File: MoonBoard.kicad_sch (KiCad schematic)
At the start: 26 parts, among them SW1 SW_SPST, U1 AMS1117-3.3, U2 STM32F446RETx, U9 SN74LV1T34DBV, Y1 25MHz

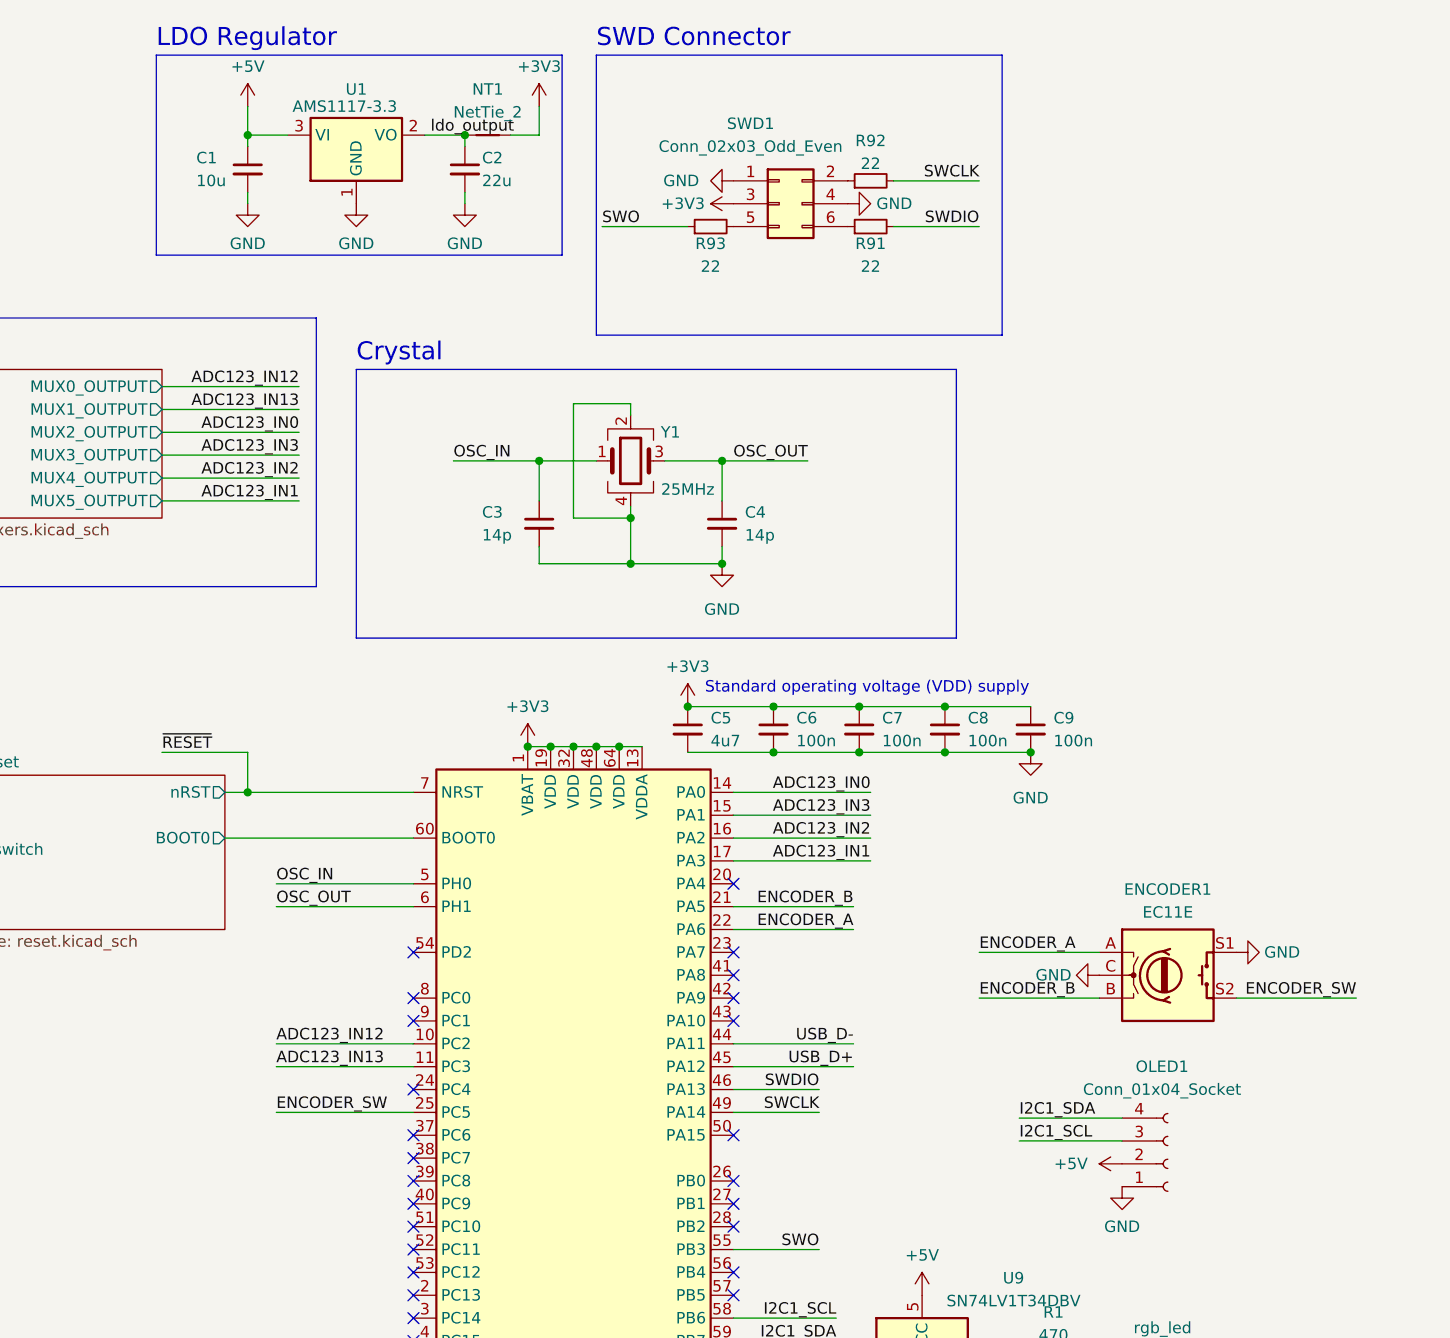
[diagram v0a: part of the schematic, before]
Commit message: fix LED footprint, add boot/reset jumpers
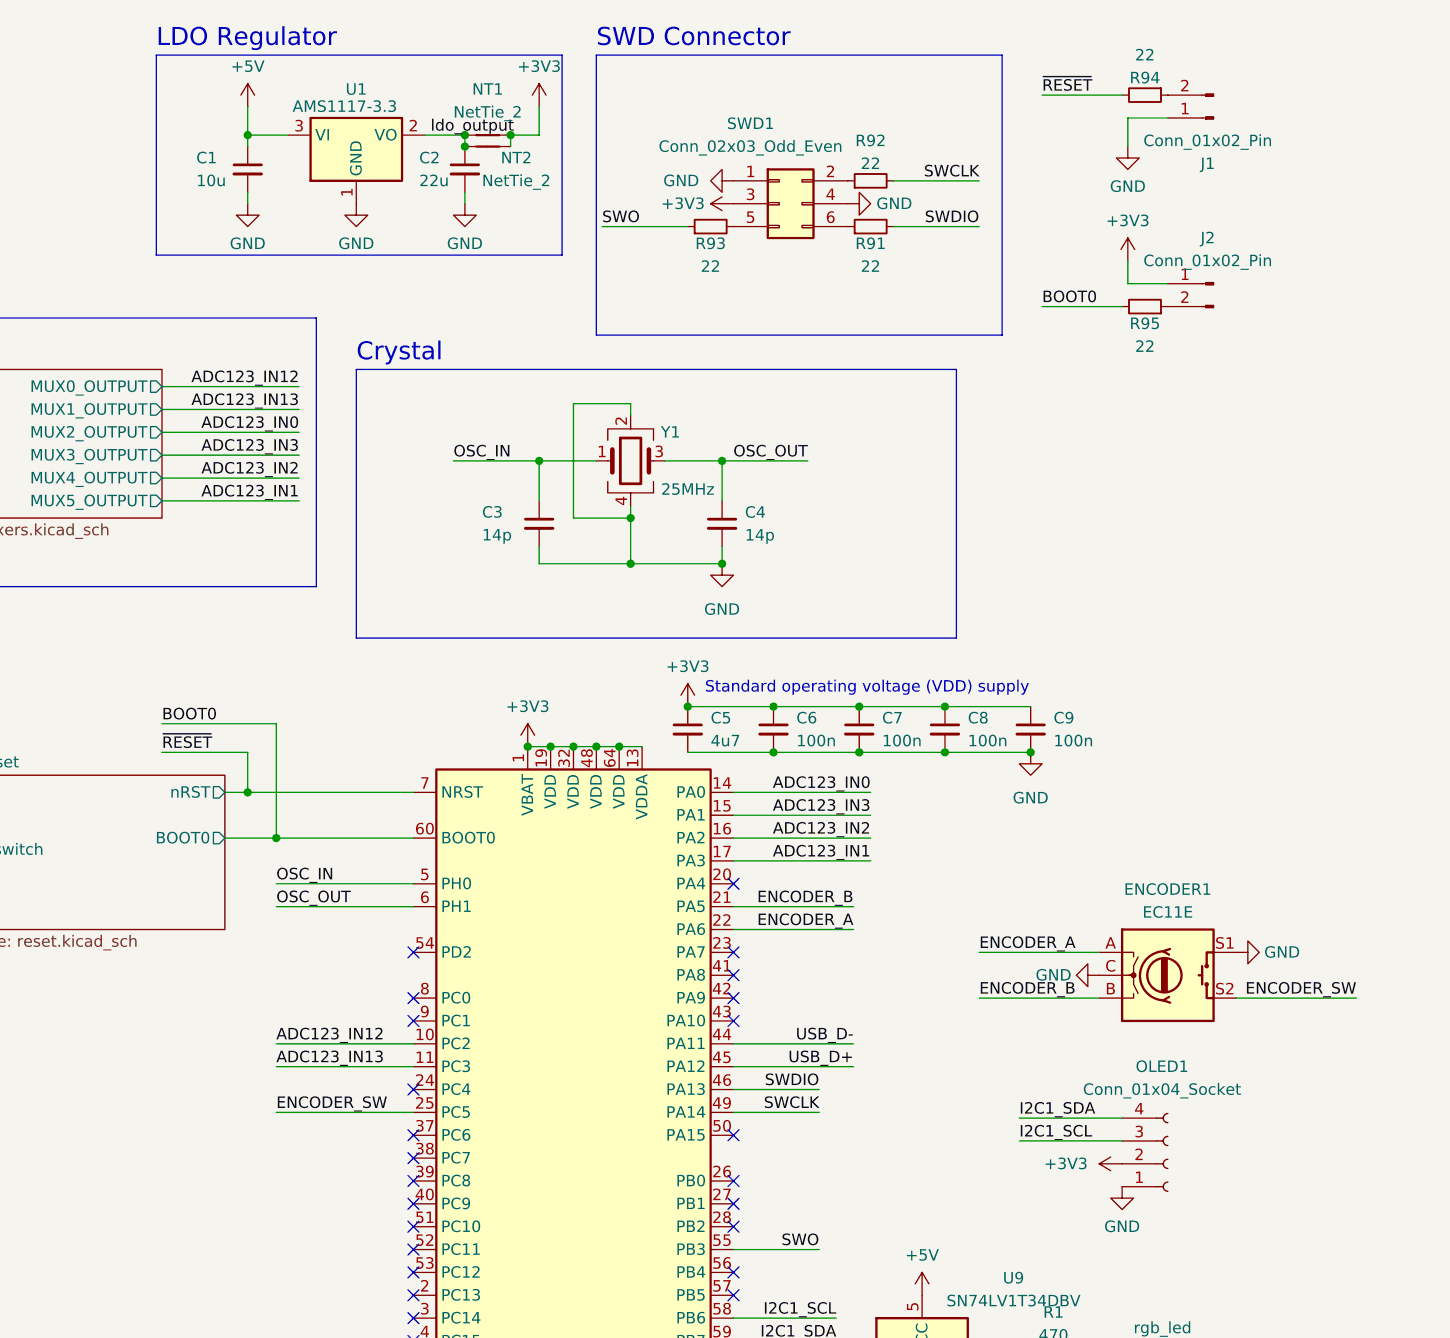
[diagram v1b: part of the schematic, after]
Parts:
- added J1, J2: Conn_01x02_Pin, Connector_PinHeader_2.54mm:PinHeader_1x02_P2.54mm_Vertical, symbol Connector:Conn_01x02_Pin
- added NT2: NetTie_2, NetTie:NetTie-2_SMD_Pad0.5mm, symbol Device:NetTie_2
- added R94, R95: 22, Resistor_SMD:R_0402_1005Metric, symbol Device:R_Small
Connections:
- net +3V3: now also OLED1.2 (Pin_2), J2.1 (Pin_1), NT2.2
- net +5V: no longer OLED1.2 (Pin_2)
- net GND: now also J1.1 (Pin_1)
- net ldo_output: now also NT2.1
- net ~{RESET}: now also R94.2
- net reset/BOOT0 renamed BOOT0
- net BOOT0: now also R95.2
- new net: J2.2 (Pin_2), R95.1
- new net: J1.2 (Pin_2), R94.1

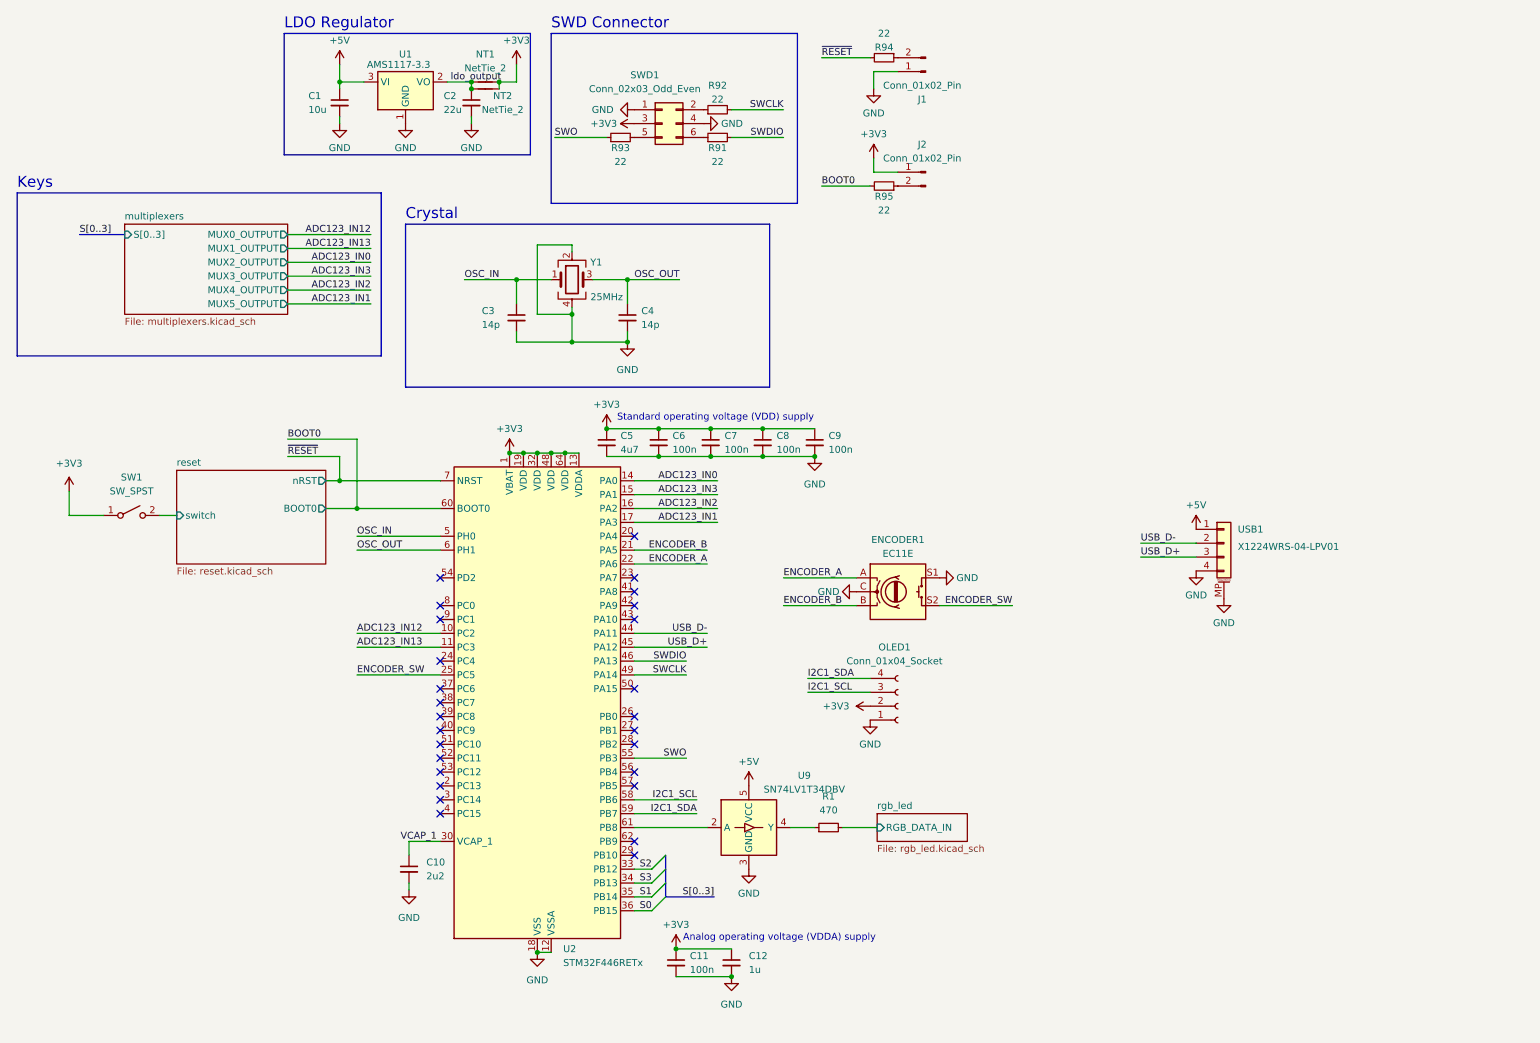
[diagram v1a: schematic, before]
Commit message: add speculative mounting holes
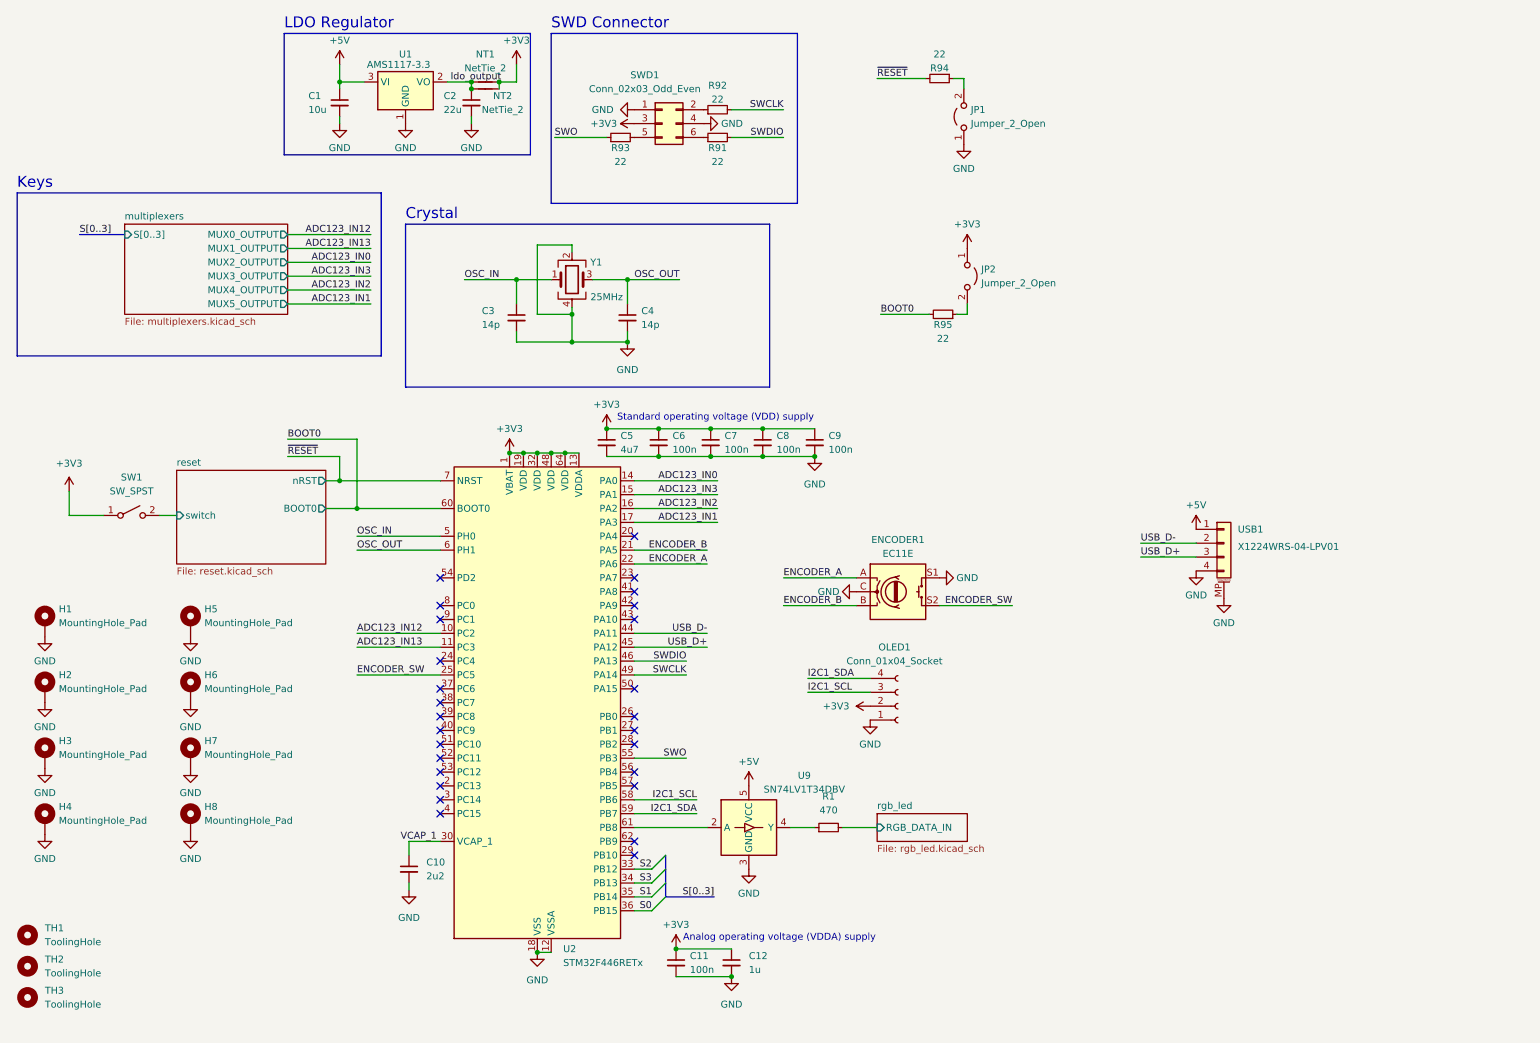
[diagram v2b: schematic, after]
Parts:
- removed J1, J2: Conn_01x02_Pin, Connector_PinHeader_2.54mm:PinHeader_1x02_P2.54mm_Vertical, symbol Connector:Conn_01x02_Pin
- added H1, H2, H3, H4, H5, H6, H7, H8: MountingHole_Pad, MountingHole:MountingHole_2.2mm_M2_Pad_Via, symbol Mechanical:MountingHole_Pad
- added JP1, JP2: Jumper_2_Open, Connector_PinHeader_2.54mm:PinHeader_1x02_P2.54mm_Vertical, symbol Jumper:Jumper_2_Open
- added TH1, TH2, TH3: ToolingHole, MoonBoard:JLC-Tooling-Hole, symbol Mechanical:MountingHole
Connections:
- net +3V3: now also JP2.1 (A)
- net GND: now also H1.1, H2.1, H3.1, H4.1, H5.1, H6.1, H7.1, H8.1, JP1.1 (A)
- net at R95.1: now also JP2.2 (B)
- net at R94.1: now also JP1.2 (B)
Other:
- moved on the sheet: R94, R95

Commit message: add reverse polarity protection to LDO
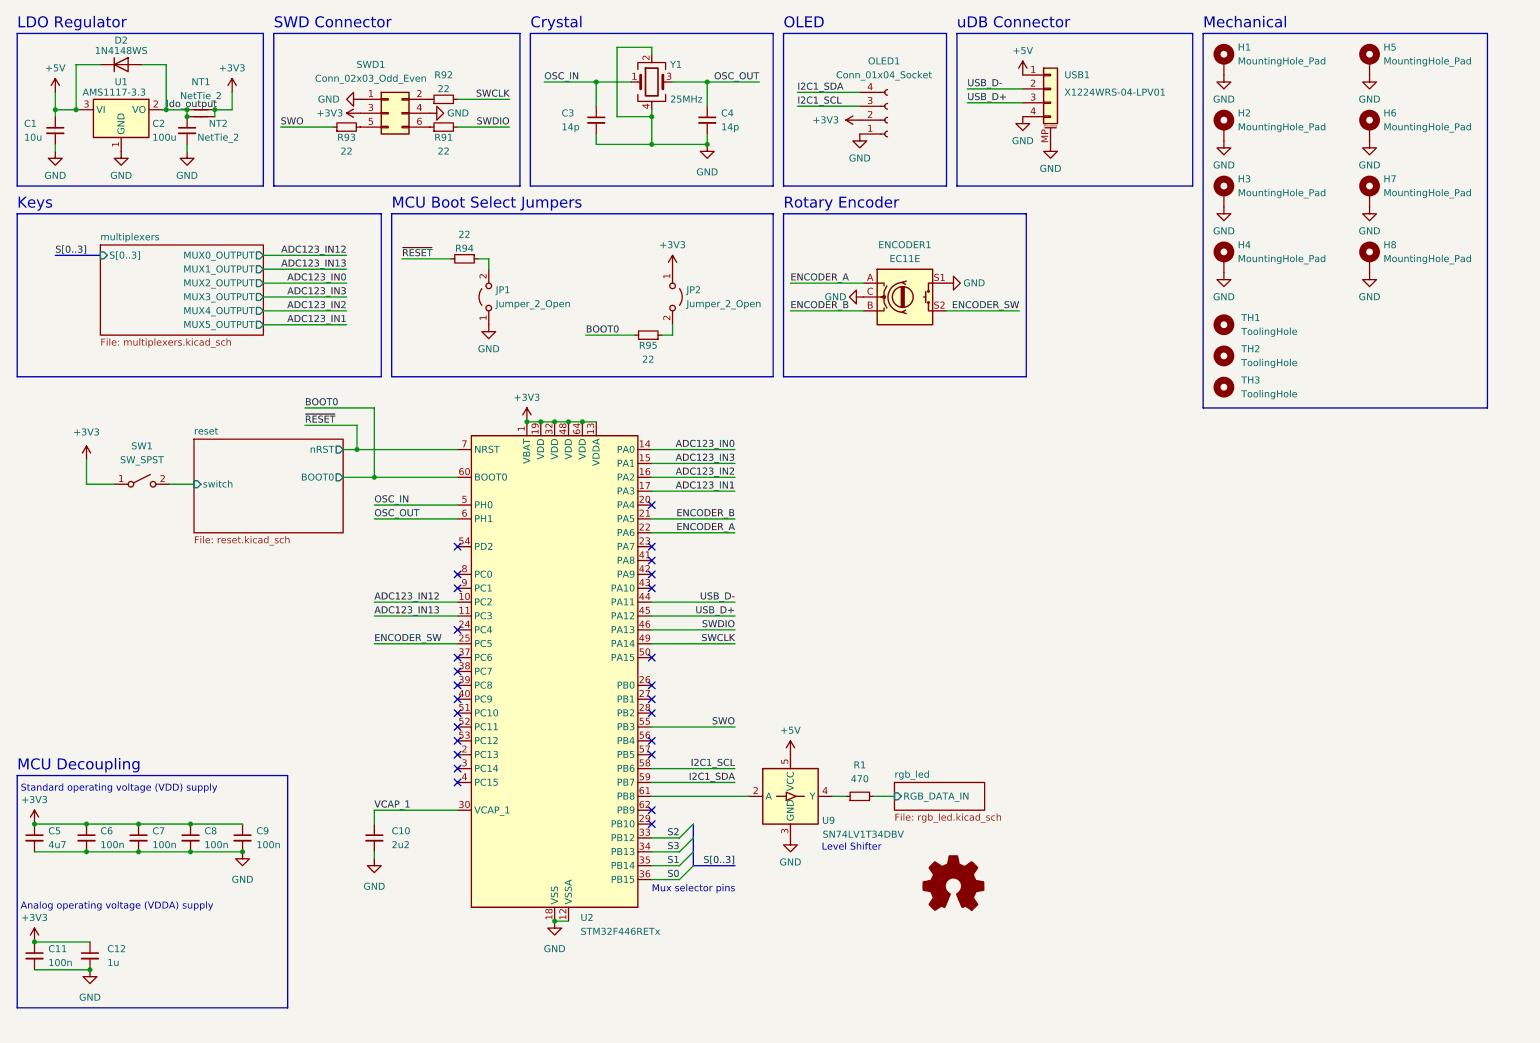
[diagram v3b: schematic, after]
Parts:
- added D2: 1N4148WS, Diode_SMD:D_SOD-323, symbol Diode:1N4148WS
- C2: value 22u -> 100u; footprint Capacitor_SMD:C_1206_3216Metric -> Capacitor_Tantalum_SMD:CP_EIA-3528-21_Kemet-B
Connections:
- net +5V: now also D2.1 (K)
- net ldo_output: now also D2.2 (A)
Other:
- note added: "Level Shifter"
- note added: "MCU Boot Select Jumpers"
- note added: "MCU Decoupling"
- note added: "Mechanical"
- note added: "Mux selector pins"
- note added: "OLED"
- note added: "Rotary Encoder"
- note added: "uDB Connector"
- title: (none) -> MoonBoard
- moved on the sheet: C1, C10, C11, C12, C2, C3, C4, C5, C6, C7, C8, C9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

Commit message: buzz
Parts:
- added BZ1: Buzzer, MoonBoard:AST1109MLTRQ, symbol Device:Buzzer
- added U3 (x2): H5VU25U, MoonBoard:DFN2510, symbol Unified-Daughterboard-rescue:TPD4E05U06DQAR-acheronSymbols
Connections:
- net ENCODER_A: now also U2.23 (PA7); no longer U2.22 (PA6)
- net ENCODER_B: now also U2.22 (PA6); no longer U2.21 (PA5)
- net GND: now also U3.3 (GND), U3.3 (GND), U3.8 (GND), U3.8 (GND)
- net I2C1_SCL: now also U3.5 (D2-), U3.6 (NC)
- net I2C1_SDA: now also U3.4 (D2+), U3.7 (NC)
- net USB_D+: now also U3.1 (IO1), U3.10 (NC)
- net USB_D-: now also U3.2 (IO2), U3.9 (NC)
- net BUZZ+: now reaches U2.20 (PA4)
- net BUZZ+: now also BZ1.1 (-)
- new net: U3.1 (IO1), U3.10 (NC)
- new net: U3.2 (IO2), U3.9 (NC)
- new net: U3.4 (D2+), U3.7 (NC)
- new net: U3.5 (D2-), U3.6 (NC)
- new net BUZZ-: BZ1.2 (+), U2.21 (PA5)
- no-connect marks 27 -> 29
